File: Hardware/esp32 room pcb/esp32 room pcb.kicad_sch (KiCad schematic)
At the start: 6 parts, among them J1 DISPLAY connector, J2 BATTERY connector, Q1 AO3400A, SW1 SW_Wuerth_450301014042

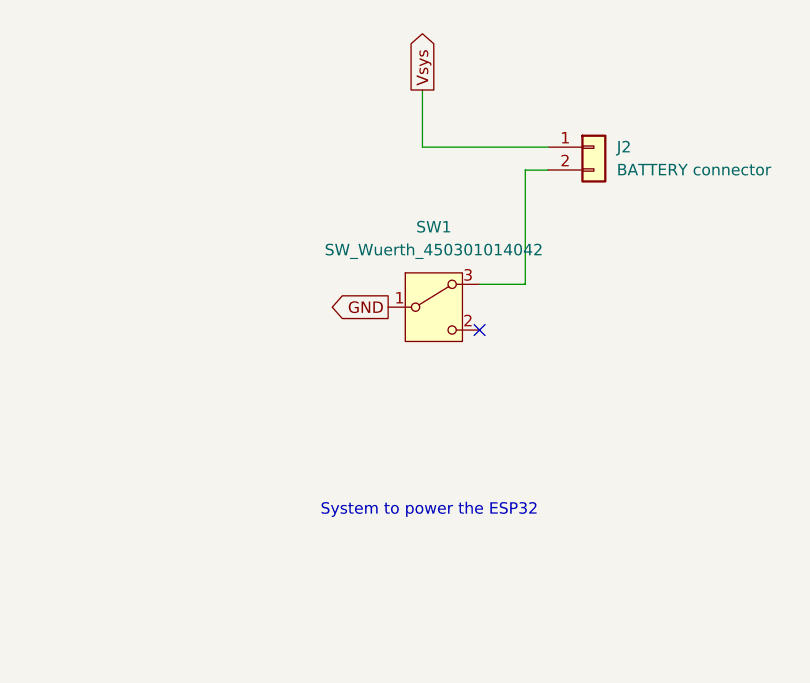
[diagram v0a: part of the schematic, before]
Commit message: modification of the switch to a cheaper on
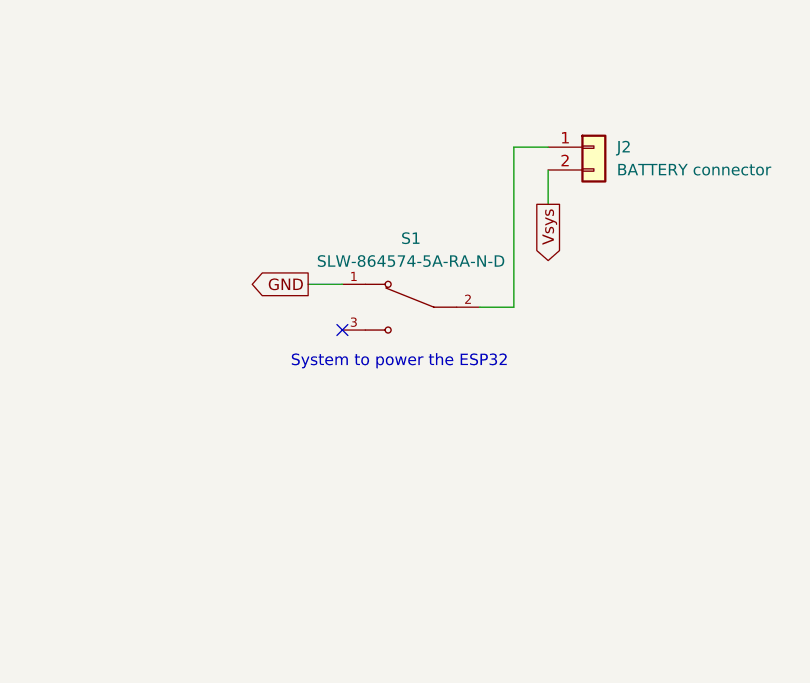
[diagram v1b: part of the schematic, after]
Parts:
- removed SW1: SW_Wuerth_450301014042, Button_Switch_THT:SW_Slide-03_Wuerth-WS-SLTV_10x2.5x6.4_P2.54mm, symbol Switch:SW_Wuerth_450301014042
- added S1: SLW-864574-5A-RA-N-D, Library:SW_SLW-864574-5A-RA-N-D, symbol SLW-864574-5A-RA-N-D:SLW-864574-5A-RA-N-D
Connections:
- net GND: now also S1.1
- net Vsys: now also J2.2 (Pin_2); no longer J2.1 (Pin_1)
- new net: J2.1 (Pin_1), S1.2

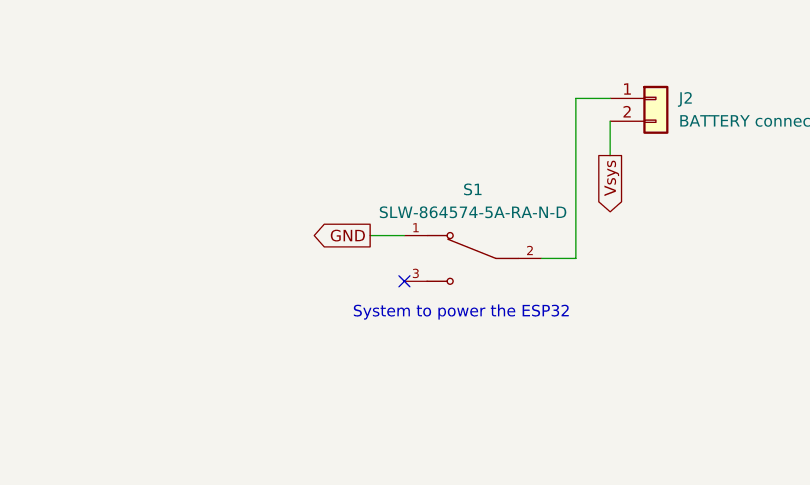
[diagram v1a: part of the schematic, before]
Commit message: corection et modification des bugs du à la basse tension (PCB + Arduino)
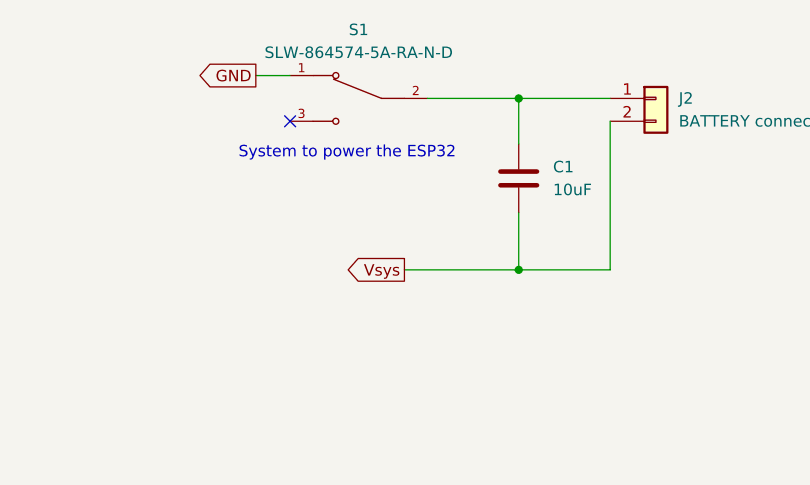
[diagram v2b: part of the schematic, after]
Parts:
- added C1: 10uF, Capacitor_SMD:C_0805_2012Metric, symbol Device:C
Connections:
- net Vsys: now also C1.2
- net at J2.1 (Pin_1), S1.2: now also C1.1
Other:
- moved on the sheet: S1
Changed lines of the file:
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@@
 	(text "System to power the ESP32 "
 		(exclude_from_sim no)
-		(at 220.98 64.516 0)
+		(at 208.28 46.736 0)
 		(effects
 			(font
@@
 		)
 	)
+	(junction
+		(at 227.33 59.69)
+		(diameter 0)
+		(color 0 0 0 0)
+	)
+	(junction
+		(at 227.33 40.64)
+		(diameter 0)
+		(color 0 0 0 0)
+	)
 	(no_connect
 		(at 106.68 125.73)
@@
 	)
 	(no_connect
-		(at 214.63 60.96)
+		(at 201.93 43.18)
 	)
 	(no_connect
@@
 	(wire
 		(pts
-			(xy 237.49 43.18) (xy 237.49 46.99)
+			(xy 237.49 59.69) (xy 227.33 59.69)
 		)
 		(stroke
@@
 	(wire
 		(pts
-			(xy 210.82 55.88) (xy 214.63 55.88)
+			(xy 227.33 53.34) (xy 227.33 59.69)
 		)
 		(stroke
@@
 	(wire
 		(pts
-			(xy 229.87 58.42) (xy 233.68 58.42)
+			(xy 227.33 59.69) (xy 214.63 59.69)
 		)
 		(stroke
@@
 	(wire
 		(pts
-			(xy 237.49 40.64) (xy 233.68 40.64)
+			(xy 227.33 40.64) (xy 237.49 40.64)
 		)
 		(stroke
@@
 	(wire
 		(pts
-			(xy 233.68 40.64) (xy 233.68 58.42)
+			(xy 237.49 43.18) (xy 237.49 59.69)
 		)
 		(stroke
@@
 		)
 	)
+	(wire
+		(pts
+			(xy 198.12 38.1) (xy 201.93 38.1)
+		)
+		(stroke
+			(width 0)
+			(type default)
+		)
+	)
+	(wire
+		(pts
+			(xy 227.33 40.64) (xy 227.33 45.72)
+		)
+		(stroke
+			(width 0)
+			(type default)
+		)
+	)
+	(wire
+		(pts
+			(xy 217.17 40.64) (xy 227.33 40.64)
+		)
+		(stroke
+			(width 0)
+			(type default)
+		)
+	)
 	(global_label "GND"
 		(shape bidirectional)
@@
 	(global_label "Vsys"
 		(shape output)
-		(at 237.49 46.99 270)
-		(fields_autoplaced yes)
-		(effects
-			(font
-				(size 1.27 1.27)
-			)
-			(justify right)
-		)
-		(property "Intersheetrefs" "${INTERSHEET_REFS}"
-			(at 237.49 54.0876 90)
+		(at 214.63 59.69 180)
+		(fields_autoplaced yes)
+		(effects
+			(font
+				(size 1.27 1.27)
+			)
+			(justify right)
+		)
+		(property "Intersheetrefs" "${INTERSHEET_REFS}"
+			(at 207.5324 59.69 0)
 			(effects
 				(font
@@
 	(global_label "GND"
 		(shape output)
-		(at 210.82 55.88 180)
-		(fields_autoplaced yes)
-		(effects
-			(font
-				(size 1.27 1.27)
-			)
-			(justify right)
-		)
-		(property "Intersheetrefs" "${INTERSHEET_REFS}"
-			(at 203.9643 55.88 0)
+		(at 198.12 38.1 180)
+		(fields_autoplaced yes)
+		(effects
+			(font
+				(size 1.27 1.27)
+			)
+			(justify right)
+		)
+		(property "Intersheetrefs" "${INTERSHEET_REFS}"
+			(at 191.2643 38.1 0)
 			(effects
 				(font
@@
 	(symbol
 		(lib_id "SLW-864574-5A-RA-N-D:SLW-864574-5A-RA-N-D")
-		(at 222.25 58.42 0)
+		(at 209.55 40.64 0)
 		(mirror y)
 		(unit 1)
@@
 		(dnp no)
 		(property "Reference" "S1"
-			(at 222.25 50.8 0)
+			(at 209.55 33.02 0)
 			(effects
 				(font
@@
 		)
 		(property "Value" "SLW-864574-5A-RA-N-D"
-			(at 222.25 53.34 0)
+			(at 209.55 35.56 0)
 			(effects
 				(font
@@
 		)
 		(property "Footprint" "Library:SW_SLW-864574-5A-RA-N-D"
-			(at 222.25 58.42 0)
+			(at 209.55 40.64 0)
 			(effects
 				(font
@@
 		)
 		(property "Datasheet" ""
-			(at 222.25 58.42 0)
+			(at 209.55 40.64 0)
 			(effects
 				(font
@@
 		)
 		(property "Description" ""
-			(at 222.25 58.42 0)
+			(at 209.55 40.64 0)
 			(effects
 				(font
@@
 		)
 		(property "MF" "Same Sky"
-			(at 222.25 58.42 0)
+			(at 209.55 40.64 0)
 			(effects
 				(font
@@
 		)
 		(property "Description_1" "8.6 x 4.5 x 6.2 mm, 5 mm Raised Slide Actuator, Right Angle, Through Hole, Slide Switch"
-			(at 222.25 58.42 0)
+			(at 209.55 40.64 0)
 			(effects
 				(font
@@
 		)
 		(property "Package" "None"
-			(at 222.25 58.42 0)
+			(at 209.55 40.64 0)
 			(effects
 				(font
@@
 		)
 		(property "Price" "None"
-			(at 222.25 58.42 0)
+			(at 209.55 40.64 0)
 			(effects
 				(font
@@
 		)
 		(property "Check_prices" "https://www.snapeda.com/parts/SLW-864574-5A-RA-N-D/Same+Sky/view-part/?ref=eda"
-			(at 222.25 58.42 0)
+			(at 209.55 40.64 0)
 			(effects
 				(font
@@
 		)
 		(property "STANDARD" "Manufacturer Recommendations"
-			(at 222.25 58.42 0)
+			(at 209.55 40.64 0)
 			(effects
 				(font
@@
 		)
 		(property "PARTREV" "1.01"
-			(at 222.25 58.42 0)
+			(at 209.55 40.64 0)
 			(effects
 				(font
@@
 		)
 		(property "SnapEDA_Link" "https://www.snapeda.com/parts/SLW-864574-5A-RA-N-D/Same+Sky/view-part/?ref=snap"
-			(at 222.25 58.42 0)
+			(at 209.55 40.64 0)
 			(effects
 				(font
@@
 		)
 		(property "MP" "SLW-864574-5A-RA-N-D"
-			(at 222.25 58.42 0)
+			(at 209.55 40.64 0)
 			(effects
 				(font
@@
 		)
 		(property "Availability" "In Stock"
-			(at 222.25 58.42 0)
+			(at 209.55 40.64 0)
 			(effects
 				(font
@@
 		)
 		(property "MANUFACTURER" "Same Sky"
-			(at 222.25 58.42 0)
+			(at 209.55 40.64 0)
 			(effects
 				(font
@@
 					(unit 1)
 				)
+			)
+		)
+	)
+	(symbol
+		(lib_id "Device:C")
+		(at 227.33 49.53 0)
+		(unit 1)
+		(exclude_from_sim no)
+		(in_bom yes)
+		(on_board yes)
+		(dnp no)
+		(fields_autoplaced yes)
+		(property "Reference" "C1"
+			(at 231.14 48.2599 0)
+			(effects
+				(font
+					(size 1.27 1.27)
+				)
+				(justify left)
+			)
+		)
+		(property "Value" "10uF"
+			(at 231.14 50.7999 0)
+			(effects
+				(font
+					(size 1.27 1.27)
+				)
+				(justify left)
+			)
+		)
+		(property "Footprint" "Capacitor_SMD:C_0805_2012Metric"
+			(at 228.2952 53.34 0)
+			(effects
+				(font
+					(size 1.27 1.27)
+				)
+				(hide yes)
+			)
+		)
+		(property "Datasheet" "~"
+			(at 227.33 49.53 0)
+			(effects
+				(font
+					(size 1.27 1.27)
+				)
+				(hide yes)
+			)
+		)
+		(property "Description" "Unpolarized capacitor"
+			(at 227.33 49.53 0)
+			(effects
+				(font
+					(size 1.27 1.27)
+				)
+				(hide yes)
+			)
+		)
+		(pin "1"
+		)
+		(pin "2"
+		)
+		(instances
+			(project ""
+				(path "/5785d8ed-438b-4398-9b9b-75da588fdcbe"
+					(reference "C1")
+					(unit 1)
+				)

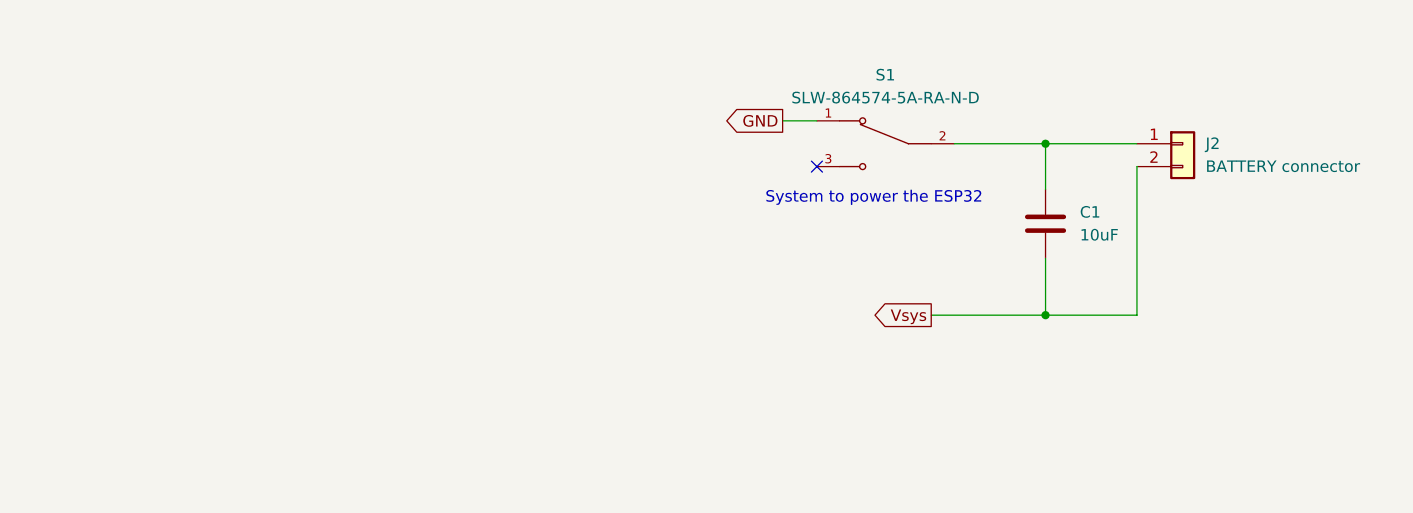
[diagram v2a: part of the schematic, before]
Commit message: ajout d'un booster 5V pcb
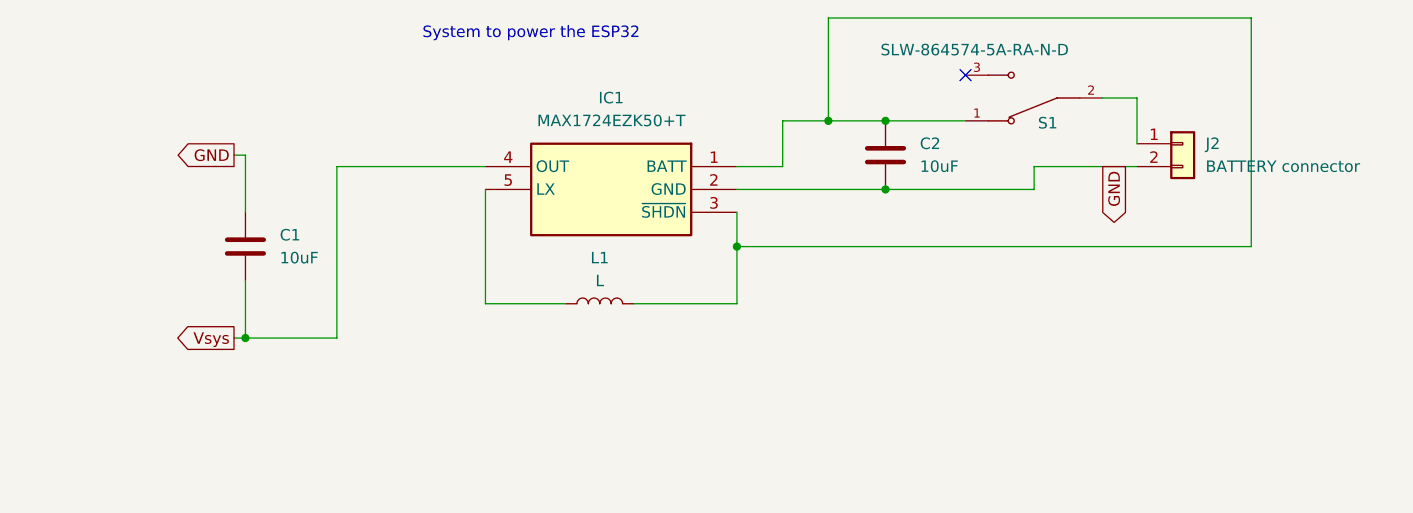
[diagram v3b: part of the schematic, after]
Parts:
- added C2: 10uF, Capacitor_SMD:C_0805_2012Metric, symbol Device:C
- added IC1: MAX1724EZK50+T, Library:SOT95P275X110-5N, symbol MAX1724EZK50+T:MAX1724EZK50+T
- added L1: L, Library:SRR1260100M, symbol Device:L
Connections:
- net GND: now also C1.1, J2.2 (Pin_2), C2.2, IC1.2 (GND); no longer S1.1
- net Vsys: now also IC1.4 (OUT); no longer J2.2 (Pin_2)
- net at J2.1 (Pin_1), S1.2: no longer C1.1
- new net: C2.1, IC1.1 (BATT), IC1.3 (~{SHDN}), L1.2, S1.1
- new net: IC1.5 (LX), L1.1
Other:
- moved on the sheet: C1, S1
